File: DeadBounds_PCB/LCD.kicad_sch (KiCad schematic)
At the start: 0 parts

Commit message: Finished schematics, assigned/made footprints except for resistors
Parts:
- added LCD1: (no value), DeadBounds Footprints:HiLetGo_ST7735, symbol DeadBounds_Symbols:HiLetgo_ST7735
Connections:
- new net +3.3V: LCD1.15 (VCC), LCD1.2 (LED+)
- new net CLK_LCD: LCD1.6 (SCK), LCD1.8 (SCL)
- new net CS_LCD: LCD1.7 (CS)
- new net D/C_LCD: LCD1.10 (A0)
- new net GND: LCD1.1 (LED-), LCD1.16 (GND)
- new net MOSI_LCD: LCD1.4 (MOSI), LCD1.9 (SDA)
- new net RESET_LCD: LCD1.11 (RESET)
- no-connect marks 0 -> 5

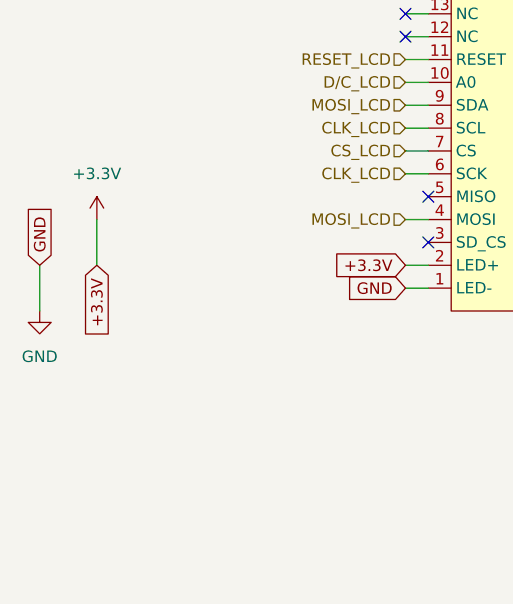
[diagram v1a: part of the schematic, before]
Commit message: MCU wiring and LED resistance edits
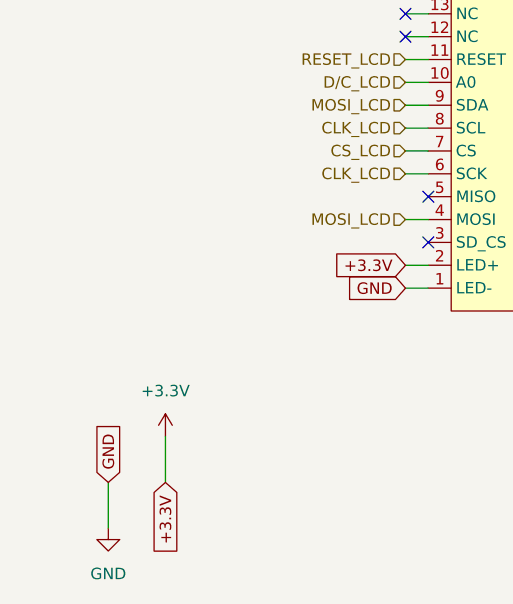
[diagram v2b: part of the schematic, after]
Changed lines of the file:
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@@
 	(wire
 		(pts
-			(xy 82.55 101.6) (xy 82.55 106.68)
+			(xy 90.17 125.73) (xy 90.17 130.81)
 		)
 		(stroke
@@
 	(wire
 		(pts
-			(xy 88.9 96.52) (xy 88.9 101.6)
+			(xy 96.52 120.65) (xy 96.52 125.73)
 		)
 		(stroke
@@
 	(global_label "+3.3V"
 		(shape input)
-		(at 88.9 101.6 270)
-		(fields_autoplaced yes)
-		(effects
-			(font
-				(size 1.27 1.27)
-			)
-			(justify right)
-		)
-		(property "Intersheetrefs" "${INTERSHEET_REFS}"
-			(at 88.9 110.27 90)
+		(at 96.52 125.73 270)
+		(fields_autoplaced yes)
+		(effects
+			(font
+				(size 1.27 1.27)
+			)
+			(justify right)
+		)
+		(property "Intersheetrefs" "${INTERSHEET_REFS}"
+			(at 96.52 134.4 90)
 			(hide yes)
 			(show_name no)
@@
 	(global_label "GND"
 		(shape input)
-		(at 82.55 101.6 90)
+		(at 90.17 125.73 90)
 		(fields_autoplaced yes)
 		(effects
@@
 		)
 		(property "Intersheetrefs" "${INTERSHEET_REFS}"
-			(at 82.55 94.7443 90)
+			(at 90.17 118.8743 90)
 			(hide yes)
 			(show_name no)
@@
 	(symbol
 		(lib_id "power:+3.3V")
-		(at 88.9 96.52 0)
+		(at 96.52 120.65 0)
 		(unit 1)
 		(body_style 1)
@@
 		(fields_autoplaced yes)
 		(property "Reference" "#PWR011"
-			(at 88.9 100.33 0)
+			(at 96.52 124.46 0)
 			(hide yes)
 			(show_name no)
@@
 		)
 		(property "Value" "+3.3V"
-			(at 88.9 91.44 0)
+			(at 96.52 115.57 0)
 			(show_name no)
 			(do_not_autoplace no)
@@
 		)
 		(property "Footprint" ""
-			(at 88.9 96.52 0)
+			(at 96.52 120.65 0)
 			(hide yes)
 			(show_name no)
@@
 		)
 		(property "Datasheet" ""
-			(at 88.9 96.52 0)
+			(at 96.52 120.65 0)
 			(hide yes)
 			(show_name no)
@@
 		)
 		(property "Description" "Power symbol creates a global label with name \"+3.3V\""
-			(at 88.9 96.52 0)
+			(at 96.52 120.65 0)
 			(hide yes)
 			(show_name no)
@@
 	(symbol
 		(lib_id "power:GND")
-		(at 82.55 106.68 0)
+		(at 90.17 130.81 0)
 		(unit 1)
 		(body_style 1)
@@
 		(fields_autoplaced yes)
 		(property "Reference" "#PWR010"
-			(at 82.55 113.03 0)
+			(at 90.17 137.16 0)
 			(hide yes)
 			(show_name no)
@@
 		)
 		(property "Value" "GND"
-			(at 82.55 111.76 0)
+			(at 90.17 135.89 0)
 			(show_name no)
 			(do_not_autoplace no)
@@
 		)
 		(property "Footprint" ""
-			(at 82.55 106.68 0)
+			(at 90.17 130.81 0)
 			(hide yes)
 			(show_name no)
@@
 		)
 		(property "Datasheet" ""
-			(at 82.55 106.68 0)
+			(at 90.17 130.81 0)
 			(hide yes)
 			(show_name no)
@@
 		)
 		(property "Description" "Power symbol creates a global label with name \"GND\" , ground"
-			(at 82.55 106.68 0)
-			(hide yes)
-			(show_name no)
+			(at 90.17 130.81 0)
+			(hide yes)
+			(show_name no)

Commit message: Added footprints, made PCB. Basically done(?)
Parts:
- added J5: Conn_01x05_Socket, Connector_PinSocket_2.54mm:PinSocket_1x05_P2.54mm_Horizontal, symbol Connector:Conn_01x05_Socket
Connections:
- net CLK_LCD: now also J5.4 (Pin_4)
- net CS_LCD: now also J5.3 (Pin_3)
- net D/C_LCD: now also J5.2 (Pin_2)
- net MOSI_LCD: now also J5.5 (Pin_5)
- net RESET_LCD: now also J5.1 (Pin_1)
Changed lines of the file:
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@@
+	(wire
+		(pts
+			(xy 167.64 74.93) (xy 170.18 74.93)
+		)
+		(stroke
+			(width 0)
+			(type default)
+		)
+	)
 	(wire
 		(pts
@@
 	(wire
 		(pts
+			(xy 167.64 80.01) (xy 170.18 80.01)
+		)
+		(stroke
+			(width 0)
+			(type default)
+		)
+	)
+	(wire
+		(pts
 			(xy 123.19 66.04) (xy 125.73 66.04)
 		)
@@
 	(wire
 		(pts
+			(xy 167.64 69.85) (xy 170.18 69.85)
+		)
+		(stroke
+			(width 0)
+			(type default)
+		)
+	)
+	(wire
+		(pts
 			(xy 123.19 71.12) (xy 125.73 71.12)
 		)
@@
 	(wire
 		(pts
+			(xy 167.64 77.47) (xy 170.18 77.47)
+		)
+		(stroke
+			(width 0)
+			(type default)
+		)
+	)
+	(wire
+		(pts
 			(xy 123.19 76.2) (xy 125.73 76.2)
 		)
@@
 		(pts
 			(xy 123.19 83.82) (xy 125.73 83.82)
+		)
+		(stroke
+			(width 0)
+			(type default)
+		)
+	)
+	(wire
+		(pts
+			(xy 167.64 72.39) (xy 170.18 72.39)
 		)
 		(stroke
@@
 		)
 	)
+	(hierarchical_label "CS_LCD"
+		(shape input)
+		(at 167.64 74.93 180)
+		(effects
+			(font
+				(size 1.27 1.27)
+			)
+			(justify right)
+		)
+	)
+	(hierarchical_label "CLK_LCD"
+		(shape input)
+		(at 167.64 77.47 180)
+		(effects
+			(font
+				(size 1.27 1.27)
+			)
+			(justify right)
+		)
+	)
 	(hierarchical_label "MOSI_LCD"
 		(shape input)
@@
 	(hierarchical_label "D{slash}C_LCD"
 		(shape input)
+		(at 167.64 72.39 180)
+		(effects
+			(font
+				(size 1.27 1.27)
+			)
+			(justify right)
+		)
+	)
+	(hierarchical_label "RESET_LCD"
+		(shape input)
+		(at 167.64 69.85 180)
+		(effects
+			(font
+				(size 1.27 1.27)
+			)
+			(justify right)
+		)
+	)
+	(hierarchical_label "D{slash}C_LCD"
+		(shape input)
 		(at 123.19 81.28 180)
+		(effects
+			(font
+				(size 1.27 1.27)
+			)
+			(justify right)
+		)
+	)
+	(hierarchical_label "MOSI_LCD"
+		(shape input)
+		(at 167.64 80.01 180)
 		(effects
 			(font
@@
 					(unit 1)
 				)
+			)
+		)
+	)
+	(symbol
+		(lib_id "Connector:Conn_01x05_Socket")
+		(at 175.26 74.93 0)
+		(unit 1)
+		(body_style 1)
+		(exclude_from_sim no)
+		(in_bom yes)
+		(on_board yes)
+		(in_pos_files yes)
+		(dnp no)
+		(fields_autoplaced yes)
+		(property "Reference" "J5"
+			(at 176.53 73.6599 0)
+			(show_name no)
+			(do_not_autoplace no)
+			(effects
+				(font
+					(size 1.27 1.27)
+				)
+				(justify left)
+			)
+		)
+		(property "Value" "Conn_01x05_Socket"
+			(at 176.53 76.1999 0)
+			(show_name no)
+			(do_not_autoplace no)
+			(effects
+				(font
+					(size 1.27 1.27)
+				)
+				(justify left)
+			)
+		)
+		(property "Footprint" "Connector_PinSocket_2.54mm:PinSocket_1x05_P2.54mm_Horizontal"
+			(at 175.26 74.93 0)
+			(hide yes)
+			(show_name no)
+			(do_not_autoplace no)
+			(effects
+				(font
+					(size 1.27 1.27)
+				)
+			)
+		)
+		(property "Datasheet" ""
+			(at 175.26 74.93 0)
+			(hide yes)
+			(show_name no)
+			(do_not_autoplace no)
+			(effects
+				(font
+					(size 1.27 1.27)
+				)
+			)
+		)
+		(property "Description" "Generic connector, single row, 01x05, script generated"
+			(at 175.26 74.93 0)
+			(hide yes)
+			(show_name no)
+			(do_not_autoplace no)
+			(effects
+				(font
+					(size 1.27 1.27)
+				)
+			)
+		)
+		(pin "4"
+		)
+		(pin "1"
+		)
+		(pin "2"
+		)
+		(pin "5"
+		)
+		(pin "3"
+		)
+		(instances
+			(project "DeadBounds_PCB"
+				(path "/c652495f-dd42-4f45-9891-1e05b67942c0/f8b6db36-4902-45f1-afa6-b070f6f84c06"
+					(reference "J5")
+					(unit 1)
+				)

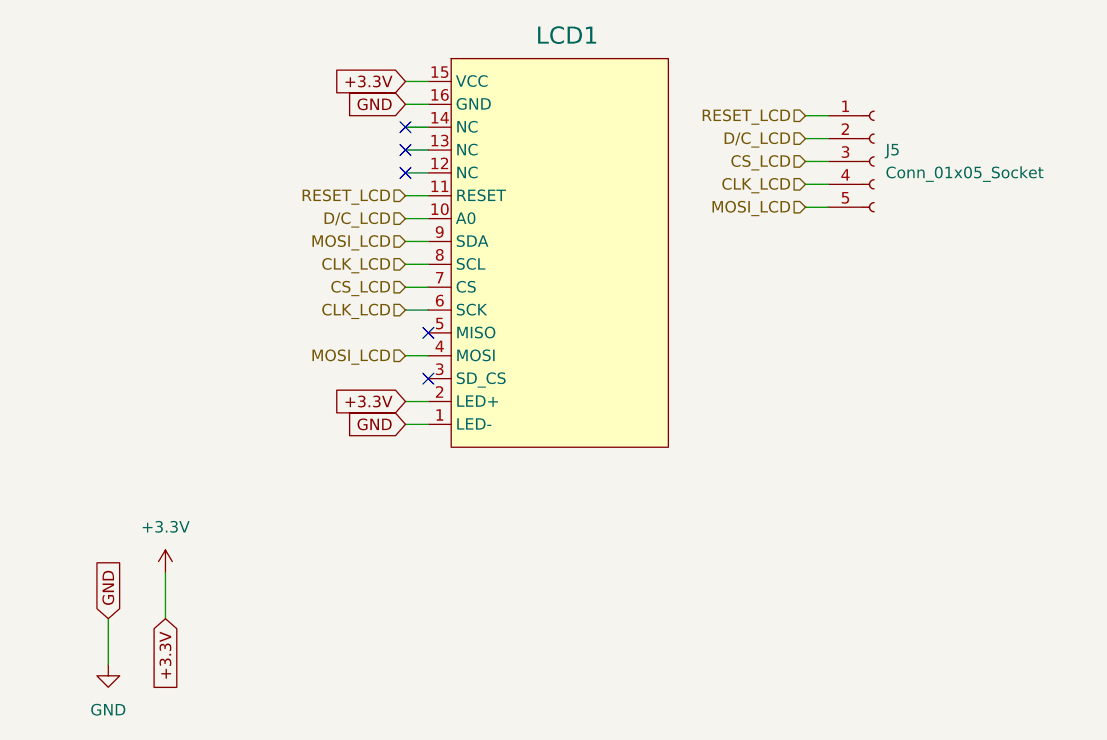
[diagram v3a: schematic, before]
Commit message: Added amplifier circuit and additional jumpers to PCB
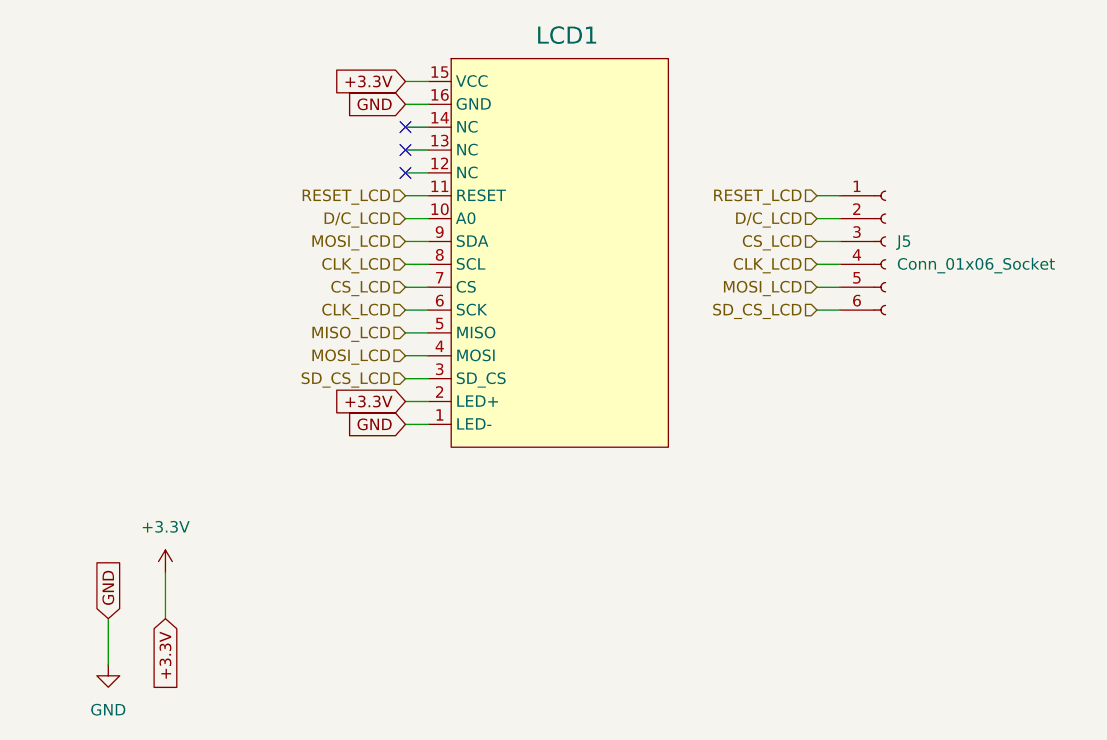
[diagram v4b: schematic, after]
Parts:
- removed J5: Conn_01x05_Socket, Connector_PinSocket_2.54mm:PinSocket_1x05_P2.54mm_Horizontal, symbol Connector:Conn_01x05_Socket
- added J5: Conn_01x06_Socket, Connector_PinSocket_2.54mm:PinSocket_1x06_P2.54mm_Horizontal, symbol Connector:Conn_01x06_Socket
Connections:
- net CLK_LCD: now also J5.4 (Pin_4)
- net CS_LCD: now also J5.3 (Pin_3)
- net D/C_LCD: now also J5.2 (Pin_2)
- net MOSI_LCD: now also J5.5 (Pin_5)
- net RESET_LCD: now also J5.1 (Pin_1)
- net SD_CS_LCD: now reaches LCD1.3 (SD_CS)
- net SD_CS_LCD: now also J5.6 (Pin_6)
- net MISO_LCD: now reaches LCD1.5 (MISO)
- no-connect marks 5 -> 3
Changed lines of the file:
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@@
 	(paper "A4")
 	(no_connect
-		(at 125.73 93.98)
-	)
-	(no_connect
-		(at 125.73 99.06)
-	)
-	(no_connect
 		(at 123.19 73.66)
 	)
@@
 	(wire
 		(pts
+			(xy 168.91 78.74) (xy 171.45 78.74)
+		)
+		(stroke
+			(width 0)
+			(type default)
+		)
+	)
+	(wire
+		(pts
 			(xy 123.19 81.28) (xy 125.73 81.28)
 		)
@@
 	(wire
 		(pts
-			(xy 167.64 74.93) (xy 170.18 74.93)
-		)
-		(stroke
-			(width 0)
-			(type default)
-		)
-	)
-	(wire
-		(pts
 			(xy 123.19 78.74) (xy 125.73 78.74)
 		)
@@
 	(wire
 		(pts
+			(xy 168.91 83.82) (xy 171.45 83.82)
+		)
+		(stroke
+			(width 0)
+			(type default)
+		)
+	)
+	(wire
+		(pts
+			(xy 168.91 91.44) (xy 171.45 91.44)
+		)
+		(stroke
+			(width 0)
+			(type default)
+		)
+	)
+	(wire
+		(pts
 			(xy 123.19 88.9) (xy 125.73 88.9)
 		)
@@
 	(wire
 		(pts
-			(xy 167.64 80.01) (xy 170.18 80.01)
+			(xy 123.19 99.06) (xy 125.73 99.06)
+		)
+		(stroke
+			(width 0)
+			(type default)
+		)
+	)
+	(wire
+		(pts
+			(xy 123.19 93.98) (xy 125.73 93.98)
 		)
 		(stroke
@@
 	(wire
 		(pts
-			(xy 167.64 69.85) (xy 170.18 69.85)
+			(xy 168.91 86.36) (xy 171.45 86.36)
 		)
 		(stroke
@@
 	(wire
 		(pts
-			(xy 167.64 77.47) (xy 170.18 77.47)
+			(xy 168.91 81.28) (xy 171.45 81.28)
 		)
 		(stroke
@@
 	(wire
 		(pts
+			(xy 168.91 88.9) (xy 171.45 88.9)
+		)
+		(stroke
+			(width 0)
+			(type default)
+		)
+	)
+	(wire
+		(pts
 			(xy 123.19 83.82) (xy 125.73 83.82)
-		)
-		(stroke
-			(width 0)
-			(type default)
-		)
-	)
-	(wire
-		(pts
-			(xy 167.64 72.39) (xy 170.18 72.39)
 		)
 		(stroke
@@
 		)
 	)
+	(hierarchical_label "D{slash}C_LCD"
+		(shape input)
+		(at 168.91 81.28 180)
+		(effects
+			(font
+				(size 1.27 1.27)
+			)
+			(justify right)
+		)
+	)
 	(hierarchical_label "CLK_LCD"
 		(shape input)
@@
 	(hierarchical_label "MOSI_LCD"
 		(shape input)
+		(at 168.91 88.9 180)
+		(effects
+			(font
+				(size 1.27 1.27)
+			)
+			(justify right)
+		)
+	)
+	(hierarchical_label "MISO_LCD"
+		(shape input)
+		(at 123.19 93.98 180)
+		(effects
+			(font
+				(size 1.27 1.27)
+			)
+			(justify right)
+		)
+	)
+	(hierarchical_label "MOSI_LCD"
+		(shape input)
 		(at 123.19 96.52 180)
 		(effects
@@
 	(hierarchical_label "CS_LCD"
 		(shape input)
-		(at 167.64 74.93 180)
+		(at 168.91 83.82 180)
+		(effects
+			(font
+				(size 1.27 1.27)
+			)
+			(justify right)
+		)
+	)
+	(hierarchical_label "SD_CS_LCD"
+		(shape input)
+		(at 168.91 91.44 180)
+		(effects
+			(font
+				(size 1.27 1.27)
+			)
+			(justify right)
+		)
+	)
+	(hierarchical_label "SD_CS_LCD"
+		(shape input)
+		(at 123.19 99.06 180)
+		(effects
+			(font
+				(size 1.27 1.27)
+			)
+			(justify right)
+		)
+	)
+	(hierarchical_label "MOSI_LCD"
+		(shape input)
+		(at 123.19 83.82 180)
 		(effects
 			(font
@@
 	(hierarchical_label "CLK_LCD"
 		(shape input)
-		(at 167.64 77.47 180)
-		(effects
-			(font
-				(size 1.27 1.27)
-			)
-			(justify right)
-		)
-	)
-	(hierarchical_label "MOSI_LCD"
-		(shape input)
-		(at 123.19 83.82 180)
+		(at 168.91 86.36 180)
 		(effects
 			(font
@@
 	(hierarchical_label "D{slash}C_LCD"
 		(shape input)
-		(at 167.64 72.39 180)
+		(at 123.19 81.28 180)
 		(effects
 			(font
@@
 	(hierarchical_label "RESET_LCD"
 		(shape input)
-		(at 167.64 69.85 180)
-		(effects
-			(font
-				(size 1.27 1.27)
-			)
-			(justify right)
-		)
-	)
-	(hierarchical_label "D{slash}C_LCD"
-		(shape input)
-		(at 123.19 81.28 180)
-		(effects
-			(font
-				(size 1.27 1.27)
-			)
-			(justify right)
-		)
-	)
-	(hierarchical_label "MOSI_LCD"
-		(shape input)
-		(at 167.64 80.01 180)
+		(at 168.91 78.74 180)
 		(effects
 			(font
@@
 	)
 	(symbol
-		(lib_id "Connector:Conn_01x05_Socket")
-		(at 175.26 74.93 0)
+		(lib_id "Connector:Conn_01x06_Socket")
+		(at 176.53 83.82 0)
 		(unit 1)
 		(body_style 1)
@@
 		(fields_autoplaced yes)
 		(property "Reference" "J5"
-			(at 176.53 73.6599 0)
+			(at 177.8 83.8199 0)
 			(show_name no)
 			(do_not_autoplace no)
@@
 			)
 		)
-		(property "Value" "Conn_01x05_Socket"
-			(at 176.53 76.1999 0)
+		(property "Value" "Conn_01x06_Socket"
+			(at 177.8 86.3599 0)
 			(show_name no)
 			(do_not_autoplace no)
@@
 			)
 		)
-		(property "Footprint" "Connector_PinSocket_2.54mm:PinSocket_1x05_P2.54mm_Horizontal"
-			(at 175.26 74.93 0)
+		(property "Footprint" "Connector_PinSocket_2.54mm:PinSocket_1x06_P2.54mm_Horizontal"
+			(at 176.53 83.82 0)
 			(hide yes)
 			(show_name no)
@@
 		)
 		(property "Datasheet" ""
-			(at 175.26 74.93 0)
-			(hide yes)
-			(show_name no)
-			(do_not_autoplace no)
-			(effects
-				(font
-					(size 1.27 1.27)
-				)
-			)
-		)
-		(property "Description" "Generic connector, single row, 01x05, script generated"
-			(at 175.26 74.93 0)
+			(at 176.53 83.82 0)
+			(hide yes)
+			(show_name no)
+			(do_not_autoplace no)
+			(effects
+				(font
+					(size 1.27 1.27)
+				)
+			)
+		)
+		(property "Description" "Generic connector, single row, 01x06, script generated"
+			(at 176.53 83.82 0)
 			(hide yes)
 			(show_name no)
@@
 		(pin "4"
 		)
+		(pin "3"
+		)
+		(pin "6"
+		)
+		(pin "5"
+		)
+		(pin "2"
+		)
 		(pin "1"
 		)
-		(pin "2"
-		)
-		(pin "5"
-		)
-		(pin "3"
-		)
 		(instances

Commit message: Added mounting holes and rerouted around joystick. PCB Ordered
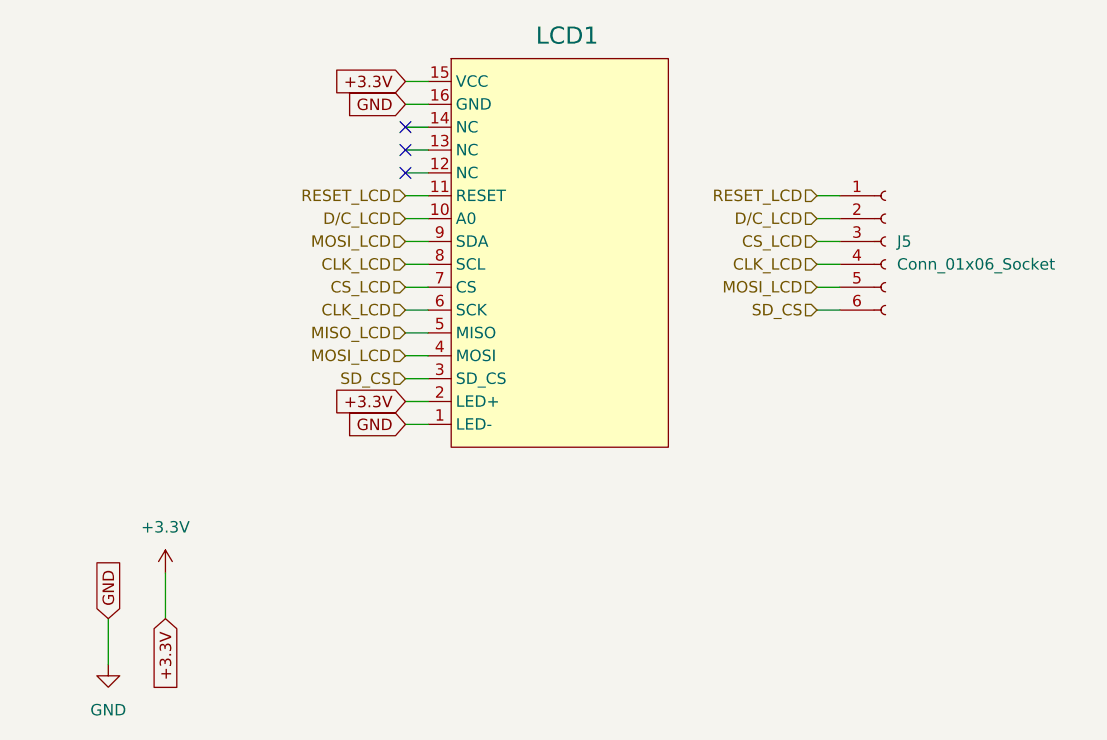
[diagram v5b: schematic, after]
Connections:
- net SD_CS_LCD renamed SD_CS
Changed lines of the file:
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@@
 		)
 	)
-	(hierarchical_label "SD_CS_LCD"
+	(hierarchical_label "SD_CS"
 		(shape input)
 		(at 168.91 91.44 180)
@@
 		)
 	)
-	(hierarchical_label "SD_CS_LCD"
+	(hierarchical_label "SD_CS"
 		(shape input)
 		(at 123.19 99.06 180)
